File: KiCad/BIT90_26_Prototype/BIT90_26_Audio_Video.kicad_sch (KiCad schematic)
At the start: 14 parts, among them Q1 2N2222, U16 Pico9918, U6 SN76489AN

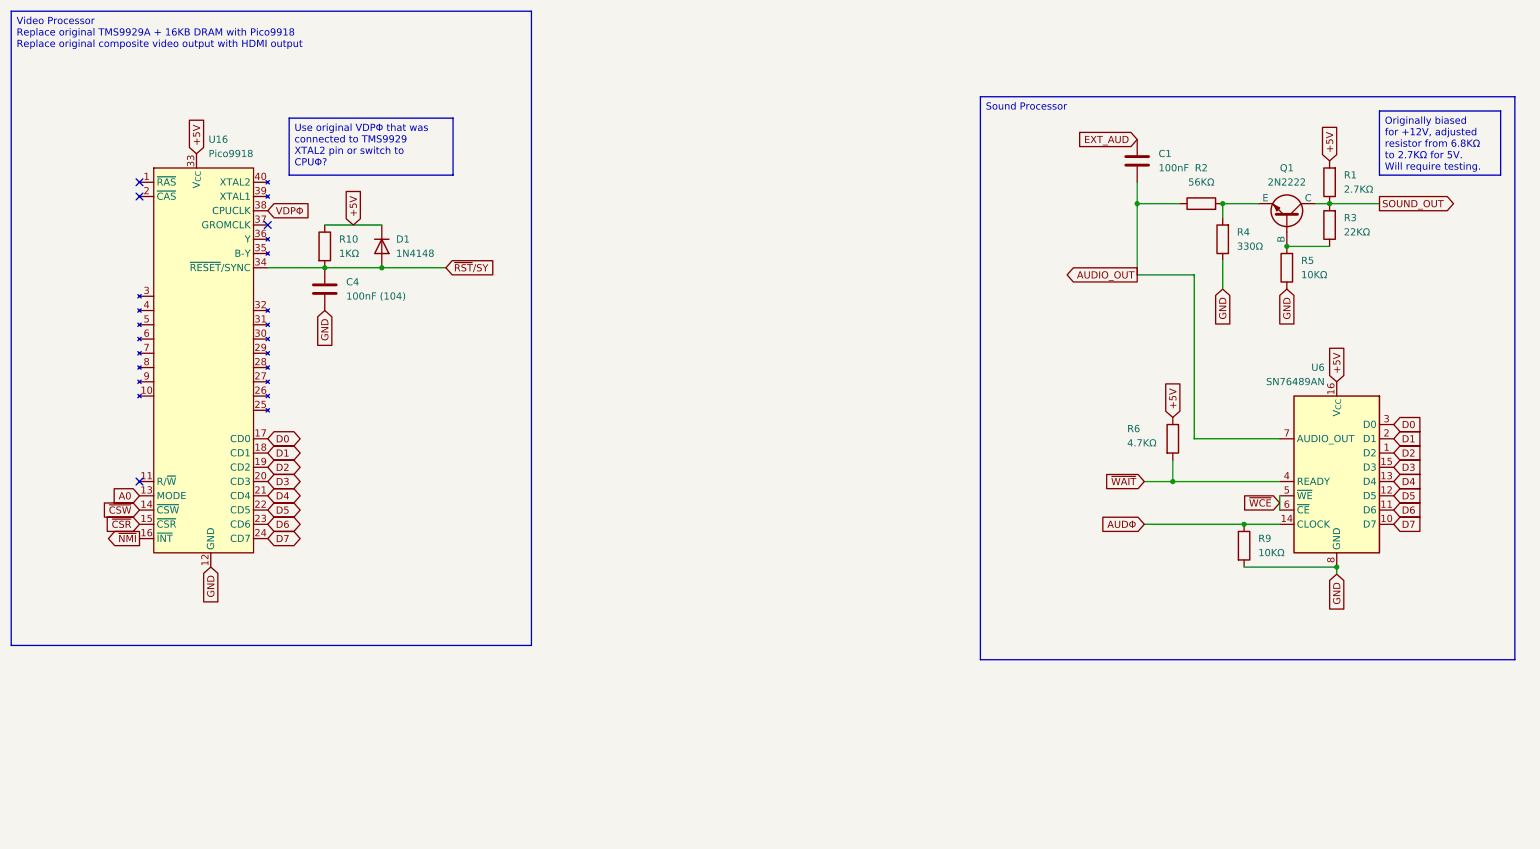
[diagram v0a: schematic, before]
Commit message: Moved initial design to Prototype folder
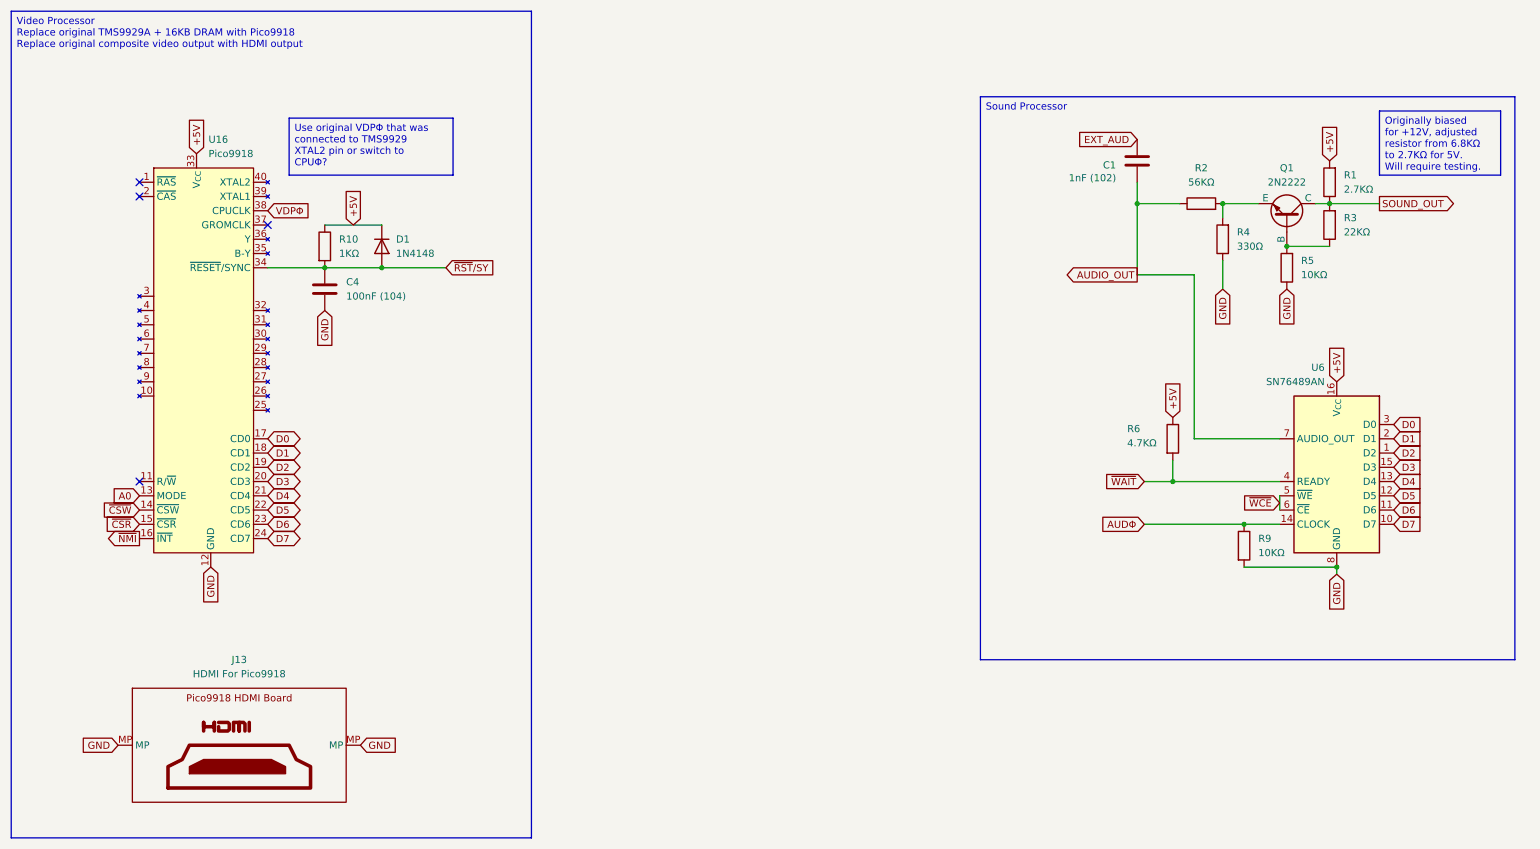
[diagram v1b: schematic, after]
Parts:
- added J13: HDMI For Pico9918, Clueless_Engineer:Pico9918_HDMI_Board, symbol Clueless_Engineer:Pico9918_HDMI_Board
- C1: value 100nF -> 1nF (102)
- D1: footprint Diode_THT:D_DO-35_SOD27_P7.62mm_Horizontal -> Clueless_Engineer:D_DO-35_SOD27_P7.62mm_Horizontal
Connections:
- net GND: now also J13.MP
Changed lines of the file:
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@@
 	(title_block
 		(title "BIT90/26 Computer - Audio & Video")
-		(date "6/JUN/2026")
-		(rev "WIP")
+		(date "7/JUN/2026")
+		(rev "PROTOTYPE")
 		(company "Brett Hallen")
 		(comment 3 "Modern recreation of the BIT90")
@@
 		(exclude_from_sim no)
 		(at 49.53 64.77 0)
-		(size 92.71 113.03)
+		(size 92.71 147.32)
 		(margins 0.9525 0.9525 0.9525 0.9525)
 		(stroke
@@
 		)
 	)
+	(global_label "GND"
+		(shape input)
+		(at 68.58 195.58 180)
+		(fields_autoplaced yes)
+		(effects
+			(font
+				(size 1.27 1.27)
+			)
+			(justify right)
+		)
+		(property "Intersheetrefs" "${INTERSHEET_REFS}"
+			(at 61.7243 195.58 0)
+			(effects
+				(font
+					(size 1.27 1.27)
+				)
+				(justify right)
+				(hide yes)
+			)
+		)
+	)
 	(global_label "D2"
 		(shape bidirectional)
@@
 		)
 	)
+	(global_label "GND"
+		(shape input)
+		(at 111.76 195.58 0)
+		(fields_autoplaced yes)
+		(effects
+			(font
+				(size 1.27 1.27)
+			)
+			(justify left)
+		)
+		(property "Intersheetrefs" "${INTERSHEET_REFS}"
+			(at 118.6157 195.58 0)
+			(effects
+				(font
+					(size 1.27 1.27)
+				)
+				(justify left)
+				(hide yes)
+			)
+		)
+	)
 	(global_label "~{NMI}"
 		(shape output)
@@
 				(justify left)
 				(hide yes)
+			)
+		)
+	)
+	(symbol
+		(lib_id "Clueless_Engineer:Pico9918_HDMI_Board")
+		(at 88.9 182.88 0)
+		(unit 1)
+		(exclude_from_sim no)
+		(in_bom yes)
+		(on_board yes)
+		(dnp no)
+		(fields_autoplaced yes)
+		(property "Reference" "J13"
+			(at 90.17 180.34 0)
+			(effects
+				(font
+					(size 1.27 1.27)
+				)
+			)
+		)
+		(property "Value" "HDMI For Pico9918"
+			(at 90.17 182.88 0)
+			(effects
+				(font
+					(size 1.27 1.27)
+				)
+			)
+		)
+		(property "Footprint" "Clueless_Engineer:Pico9918_HDMI_Board"
+			(at 88.9 182.88 0)
+			(effects
+				(font
+					(size 1.27 1.27)
+				)
+				(hide yes)
+			)
+		)
+		(property "Datasheet" ""
+			(at 88.9 182.88 0)
+			(effects
+				(font
+					(size 1.27 1.27)
+				)
+				(hide yes)
+			)
+		)
+		(property "Description" ""
+			(at 88.9 182.88 0)
+			(effects
+				(font
+					(size 1.27 1.27)
+				)
+				(hide yes)
+			)
+		)
+		(pin "MP"
+		)
+		(pin "MP"
+		)
+		(instances
+			(project "BIT90_26_Prototype"
+				(path "/d65498c3-6385-4920-ac0f-4c76daf90780/a2197f6c-13b4-44bf-8904-5835f7bd7927"
+					(reference "J13")
+					(unit 1)
+				)
 			)
 		)
@@
 			)
 		)
-		(property "Footprint" "Diode_THT:D_DO-35_SOD27_P7.62mm_Horizontal"
+		(property "Footprint" "Clueless_Engineer:D_DO-35_SOD27_P7.62mm_Horizontal"
 			(at 115.57 106.68 0)
 			(effects
@@
 		)
 		(instances
-			(project "BIT90_26"
+			(project "BIT90_26_Prototype"
 				(path "/d65498c3-6385-4920-ac0f-4c76daf90780/a2197f6c-13b4-44bf-8904-5835f7bd7927"
 					(reference "D1")
@@
 		)
 		(instances
-			(project "BIT90_26"
+			(project "BIT90_26_Prototype"
 				(path "/d65498c3-6385-4920-ac0f-4c76daf90780/a2197f6c-13b4-44bf-8904-5835f7bd7927"
 					(reference "R1")
@@
 		)
 		(instances
-			(project "BIT90_26"
+			(project "BIT90_26_Prototype"
 				(path "/d65498c3-6385-4920-ac0f-4c76daf90780/a2197f6c-13b4-44bf-8904-5835f7bd7927"
 					(reference "R2")
@@
 		)
 		(instances
-			(project "BIT90_26"
+			(project "BIT90_26_Prototype"
 				(path "/d65498c3-6385-4920-ac0f-4c76daf90780/a2197f6c-13b4-44bf-8904-5835f7bd7927"
 					(reference "R6")
@@
 		)
 		(instances
-			(project "BIT90_26"
+			(project "BIT90_26_Prototype"
 				(path "/d65498c3-6385-4920-ac0f-4c76daf90780/a2197f6c-13b4-44bf-8904-5835f7bd7927"
 					(reference "C4")
@@
 		)
 		(instances
-			(project "BIT90_26"
+			(project "BIT90_26_Prototype"
 				(path "/d65498c3-6385-4920-ac0f-4c76daf90780/a2197f6c-13b4-44bf-8904-5835f7bd7927"
 					(reference "U6")
@@
 		)
 		(instances
-			(project "BIT90_26"
+			(project "BIT90_26_Prototype"
 				(path "/d65498c3-6385-4920-ac0f-4c76daf90780/a2197f6c-13b4-44bf-8904-5835f7bd7927"
 					(reference "R3")
@@
 		)
 		(instances
-			(project "BIT90_26"
+			(project "BIT90_26_Prototype"
 				(path "/d65498c3-6385-4920-ac0f-4c76daf90780/a2197f6c-13b4-44bf-8904-5835f7bd7927"
 					(reference "U16")
@@
 		)
 		(instances
-			(project "BIT90_26"
+			(project "BIT90_26_Prototype"
 				(path "/d65498c3-6385-4920-ac0f-4c76daf90780/a2197f6c-13b4-44bf-8904-5835f7bd7927"
 					(reference "R9")
@@
 		)
 		(instances
-			(project "BIT90_26"
+			(project "BIT90_26_Prototype"
 				(path "/d65498c3-6385-4920-ac0f-4c76daf90780/a2197f6c-13b4-44bf-8904-5835f7bd7927"
 					(reference "R5")
@@
 		)
 		(instances
-			(project "BIT90_26"
+			(project "BIT90_26_Prototype"
 				(path "/d65498c3-6385-4920-ac0f-4c76daf90780/a2197f6c-13b4-44bf-8904-5835f7bd7927"
 					(reference "Q1")
@@
 		)
 		(instances
-			(project "BIT90_26"
+			(project "BIT90_26_Prototype"
 				(path "/d65498c3-6385-4920-ac0f-4c76daf90780/a2197f6c-13b4-44bf-8904-5835f7bd7927"
 					(reference "R4")
@@
 		)
 		(instances
-			(project "BIT90_26"
+			(project "BIT90_26_Prototype"
 				(path "/d65498c3-6385-4920-ac0f-4c76daf90780/a2197f6c-13b4-44bf-8904-5835f7bd7927"
 					(reference "R10")
@@
 		(on_board yes)
 		(dnp no)
-		(fields_autoplaced yes)
 		(property "Reference" "C1"
-			(at 254 90.1699 0)
-			(effects
-				(font
-					(size 1.27 1.27)
-				)
-				(justify left)
-			)
-		)
-		(property "Value" "100nF"
-			(at 254 92.7099 0)
+			(at 244.094 92.202 0)
+			(effects
+				(font
+					(size 1.27 1.27)
+				)
+				(justify left)
+			)
+		)
+		(property "Value" "1nF (102)"
+			(at 237.998 94.488 0)
 			(effects
 				(font
@@
 		)
 		(instances
-			(project "BIT90_26"
+			(project "BIT90_26_Prototype"
 				(path "/d65498c3-6385-4920-ac0f-4c76daf90780/a2197f6c-13b4-44bf-8904-5835f7bd7927"
 					(reference "C1")

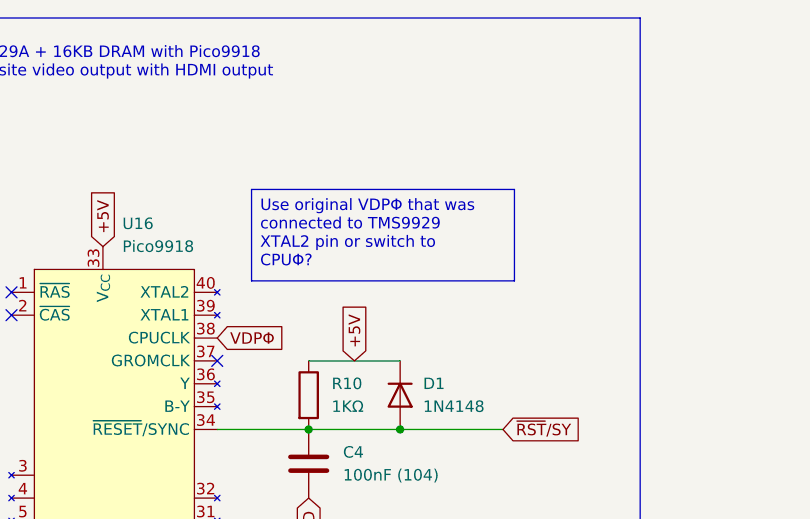
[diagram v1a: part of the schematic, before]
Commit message: Added more signal analysis to schematic
Would be nice to reduce the amount of glue logic
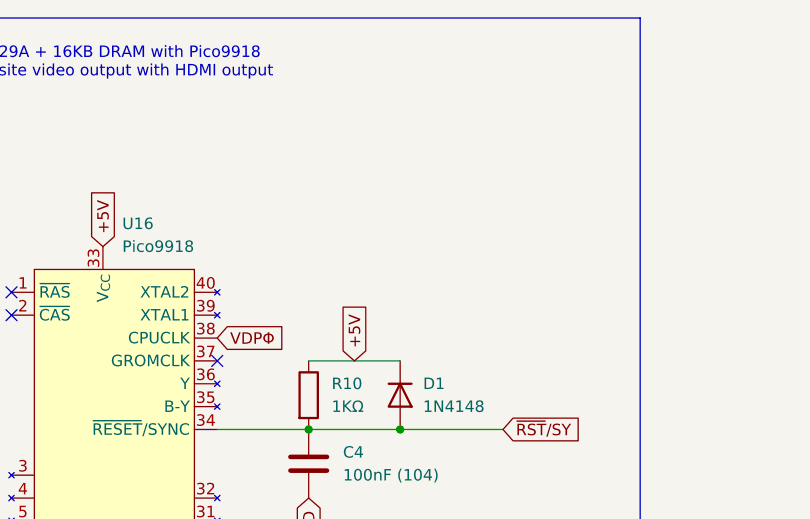
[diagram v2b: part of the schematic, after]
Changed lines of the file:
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@@
-		)
-	)
-	(text_box "Use original VDPΦ that was connected to TMS9929 XTAL2 pin or switch to CPUΦ?"
-		(exclude_from_sim no)
-		(at 99.06 83.82 0)
-		(size 29.21 10.16)
-		(margins 0.9525 0.9525 0.9525 0.9525)
-		(stroke
-			(width 0)
-			(type solid)
-		)
-		(fill
-			(type none)
-		)
-		(effects
-			(font
-				(size 1.27 1.27)
-			)
-			(justify left top)
 		)
 	)
